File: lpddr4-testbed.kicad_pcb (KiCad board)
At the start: 6 copper layers, 69.6 x 30 mm, 2 parts, among them J1 ddr4-sodimm-edge-connector, U1 MT53E256M16D1

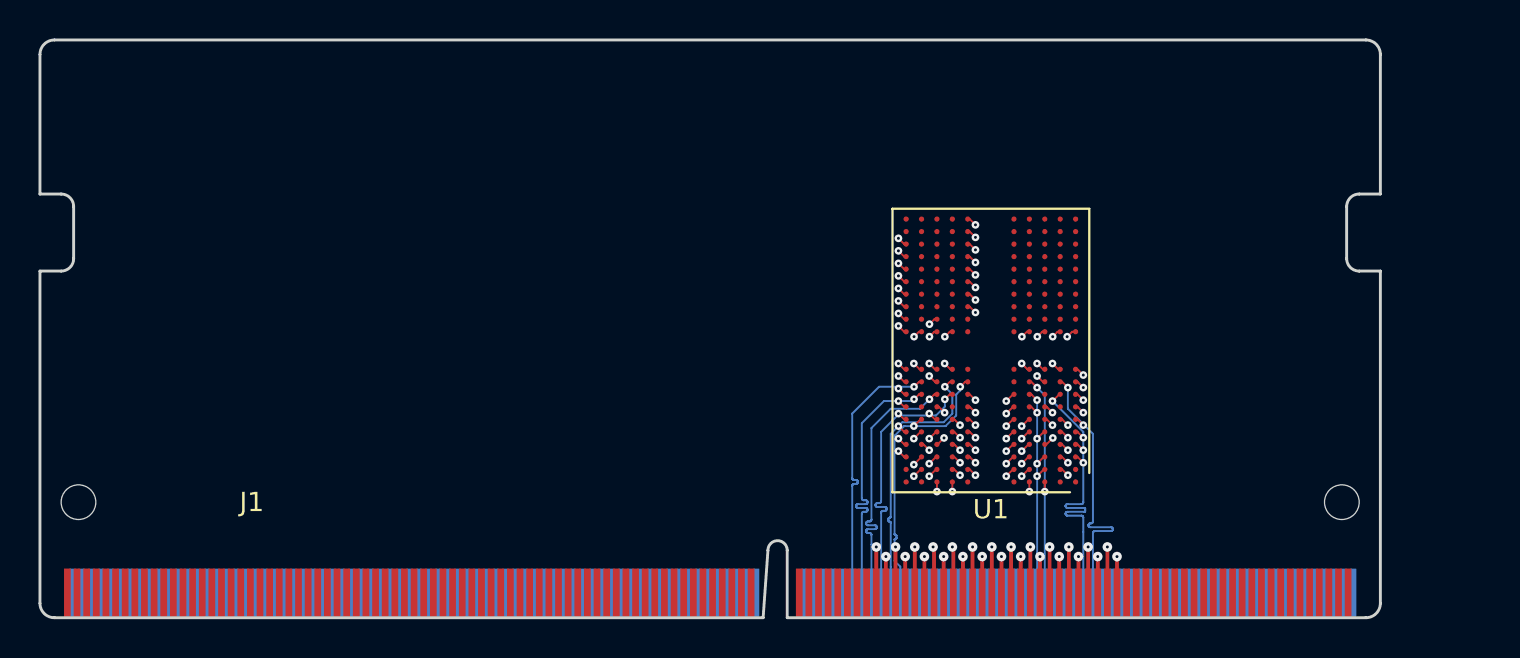
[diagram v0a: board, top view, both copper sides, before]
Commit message: Add vias for power distribution
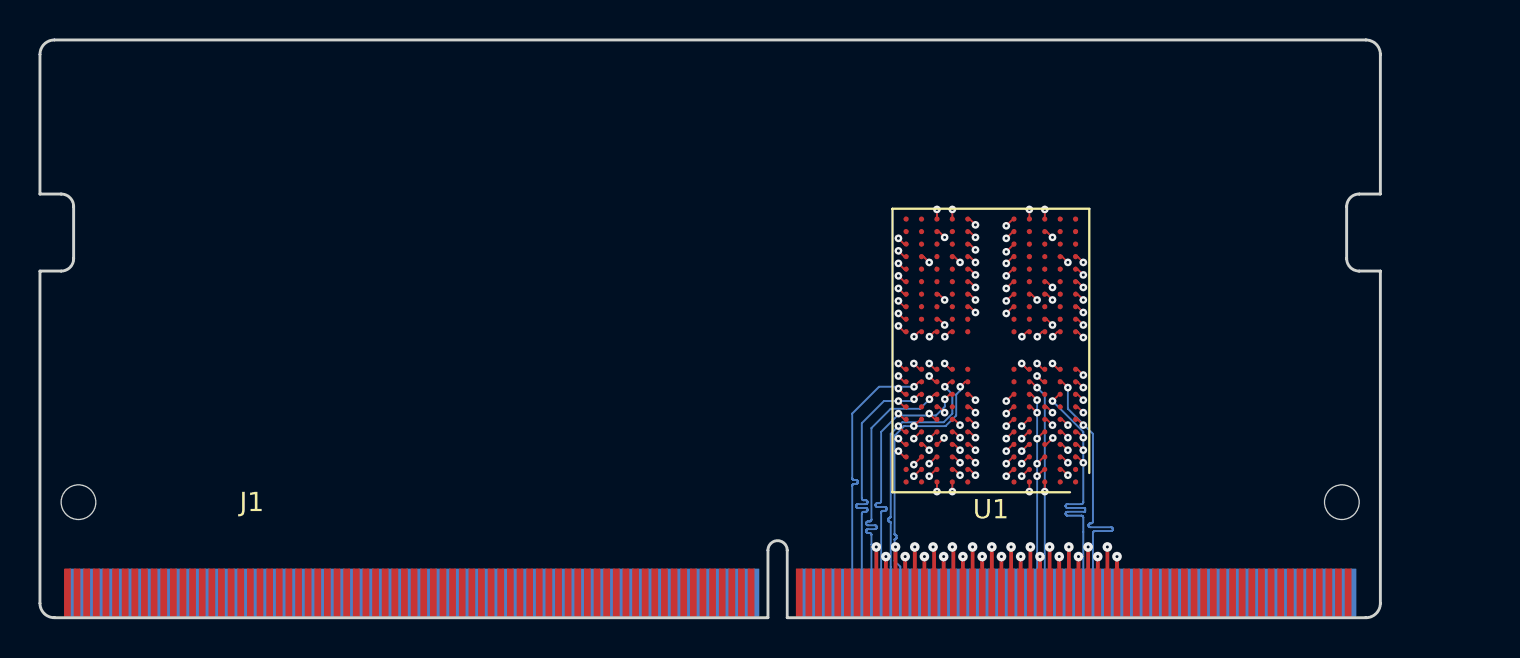
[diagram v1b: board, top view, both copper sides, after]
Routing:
- net GND: track 30.2 -> 38.1 mm, vias 45 -> 60
- net VDDQ: track 6.35 -> 9.54 mm, vias 12 -> 18
- net VDD2: track 9.92 -> 12.6 mm, vias 19 -> 24
- net VDD1: track 2.10 -> 3.15 mm, vias 4 -> 6
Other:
- outline, holes or cut-outs redrawn

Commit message: Add filtering caps to VDDQ
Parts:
- added C1: C_100n_0201, antmicro-footprints:0201-res, B.Cu at (149.8, 93.6)
- added C10: C_100n_0201, antmicro-footprints:0201-res, F.Cu at (142.2, 81.2)
- added C11: C_100n_0201, antmicro-footprints:0201-res, F.Cu at (156.6, 81.9)
- added C12: C_100n_0201, antmicro-footprints:0201-res, F.Cu at (142.3, 91.0)
- added C13: C_100n_0201, antmicro-footprints:0201-res, B.Cu at (152.6, 81.4)
- added C14: C_100n_0201, antmicro-footprints:0201-res, F.Cu at (165.2, 86.9)
- added C15: C_100n_0201, antmicro-footprints:0201-res, B.Cu at (149.4, 81.9)
- added C16: C_100n_0201, antmicro-footprints:0201-res, F.Cu at (162.8, 90.4)
- added C2: C_100n_0201, antmicro-footprints:0201-res, B.Cu at (149.4, 80.0)
- added C3: C_100n_0201, antmicro-footprints:0201-res, B.Cu at (148.9, 93.6)
- added C4: C_100n_0201, antmicro-footprints:0201-res, B.Cu at (147.0, 81.3)
- added C5: C_100n_0201, antmicro-footprints:0201-res, B.Cu at (149.4, 91.0)
- added C6: C_100n_0201, antmicro-footprints:0201-res, B.Cu at (146.3, 83.1)
- added C7: C_100n_0201, antmicro-footprints:0201-res, B.Cu at (145.6, 92.0)
- added C8: C_100n_0201, antmicro-footprints:0201-res, B.Cu at (153.3, 83.2)
- added C9: C_100n_0201, antmicro-footprints:0201-res, F.Cu at (156.4, 91.7)
- added R1: R_10k_0402, antmicro-footprints:0402-res, F.Cu at (126.5, 87.4)
- added R2: R_0R_0402, antmicro-footprints:0402-res, F.Cu at (126.5, 89.4)
- added R3: R_10k_0402, antmicro-footprints:0402-res, F.Cu at (129.4, 87.4)
- added R4: R_10k_0402, antmicro-footprints:0402-res, F.Cu at (129.4, 89.4)
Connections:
- U1 pad G2: /LPDDR4/ODT0_A -> Net-(R1-Pad2)
- U1 pad R4: Net-(U1-PadR4) -> CS0_B
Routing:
- net VDDQ: track 9.54 -> 30.7 mm, vias 18 -> 19
- net GND: track 38.1 -> 56.8 mm, vias 60 -> 62
- net CKE0_A: track 11.3 -> 12.5 mm
- net CS0_A: track 10.6 -> 11.4 mm

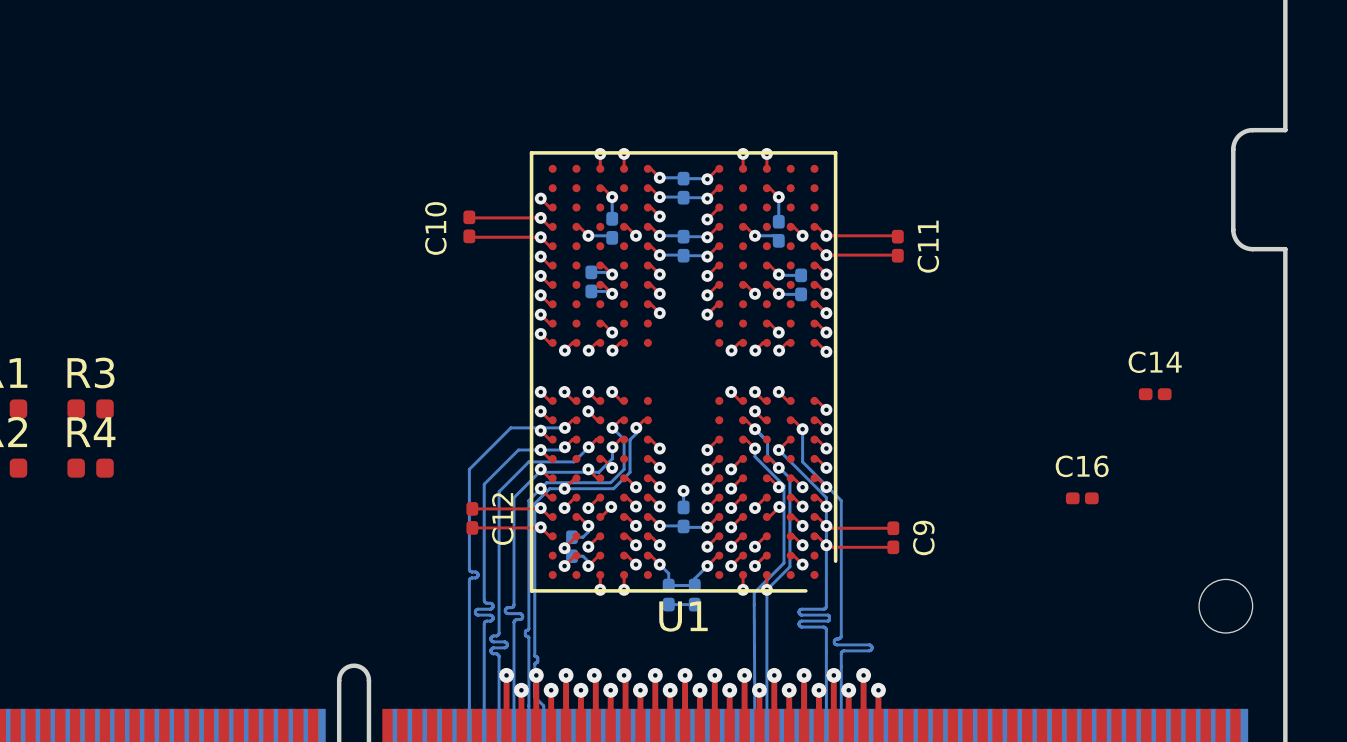
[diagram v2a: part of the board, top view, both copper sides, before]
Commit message: Add Filtering to VCC1
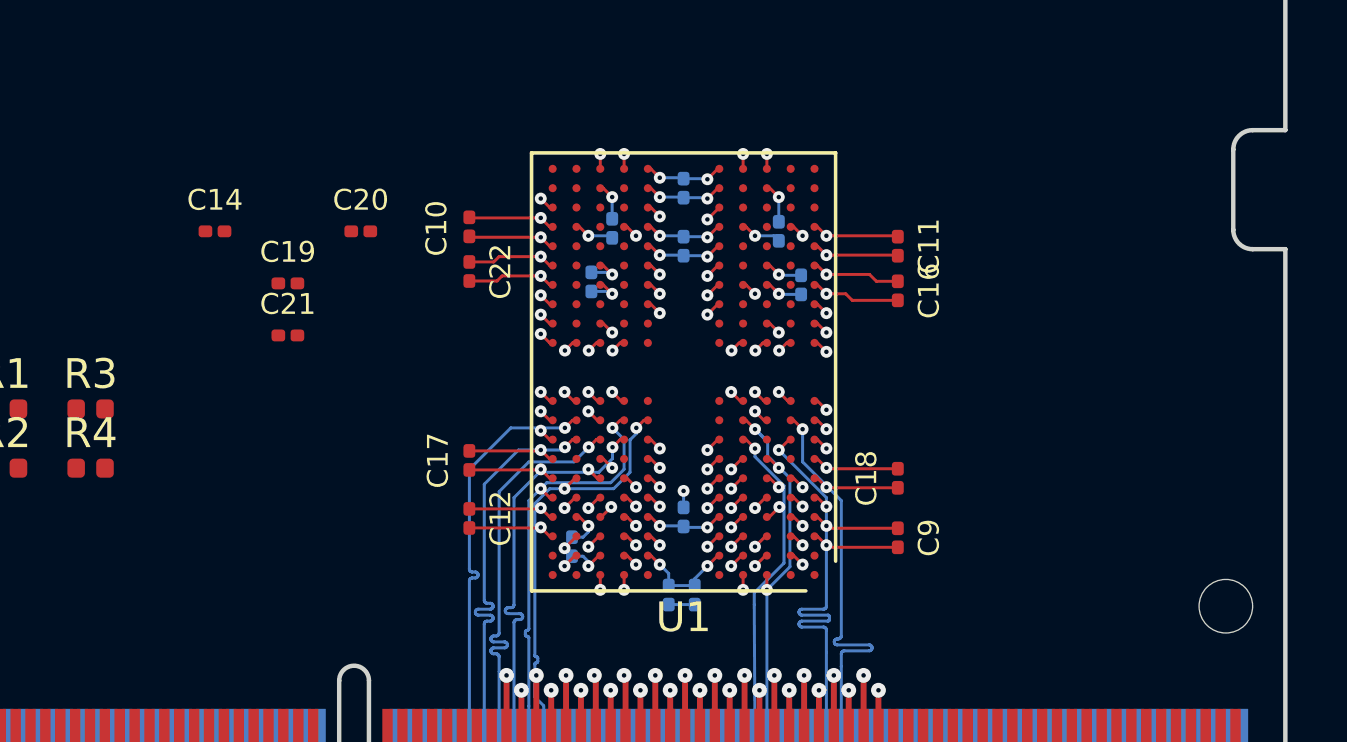
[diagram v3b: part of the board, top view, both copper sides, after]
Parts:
- added C17: C_100n_0201, antmicro-footprints:0201-res, F.Cu at (142.2, 89.1)
- added C18: C_100n_0201, antmicro-footprints:0201-res, F.Cu at (156.6, 89.7)
- added C19: C_100n_0201, antmicro-footprints:0201-res, F.Cu at (136.1, 83.2)
- added C20: C_100n_0201, antmicro-footprints:0201-res, F.Cu at (138.5, 81.4)
- added C21: C_100n_0201, antmicro-footprints:0201-res, F.Cu at (136.1, 84.9)
- added C22: C_100n_0201, antmicro-footprints:0201-res, F.Cu at (142.2, 82.8)
- moved C14 32.1 mm to (133.6, 81.4)
- moved C16 9.33 mm to (156.6, 83.4), turned to 270 degrees
- moved C9 0.15 mm to (156.6, 91.7)
- moved C12 0.10 mm to (142.2, 91.0)
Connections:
- C14 pad 1: VDDQ -> VDD1
- C16 pad 1: VDDQ -> VDD1
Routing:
- net VDD1: track 3.17 -> 13.0 mm
- net GND: track 56.8 -> 66.6 mm

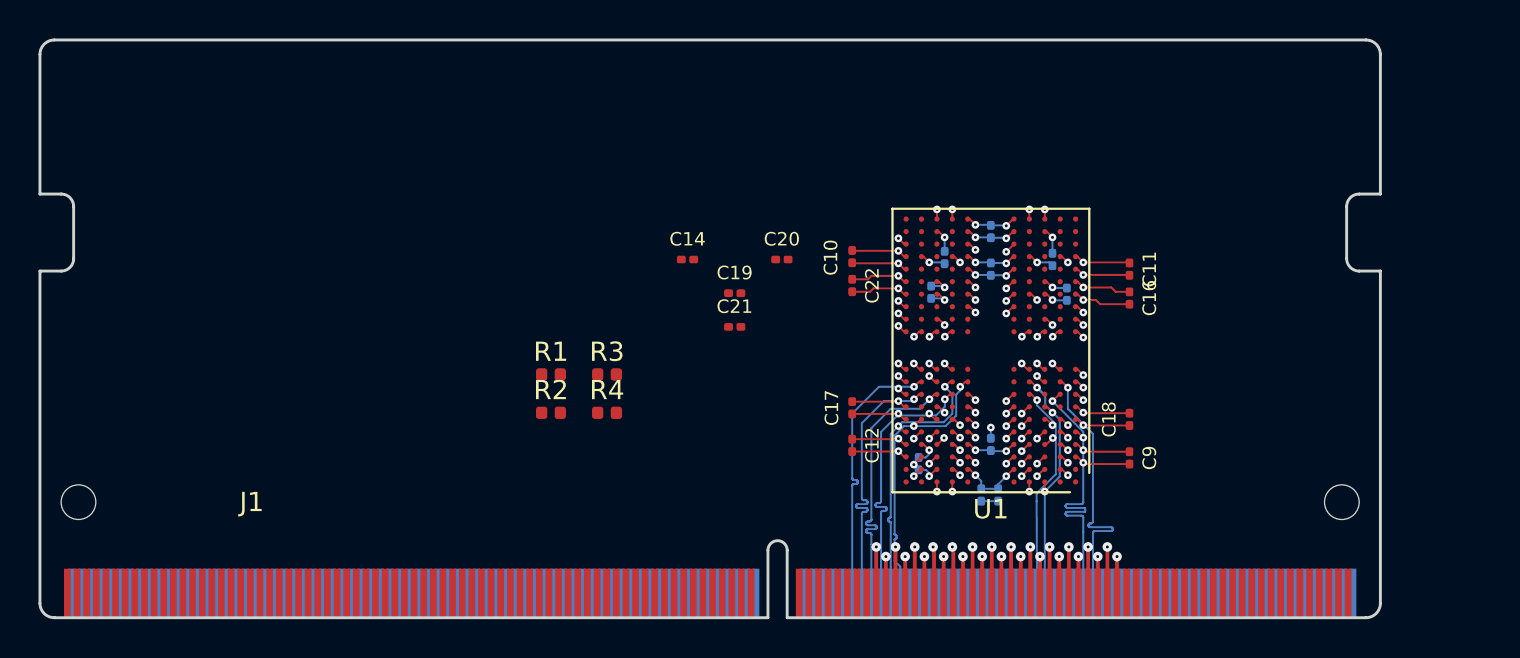
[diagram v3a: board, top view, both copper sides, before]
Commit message: Add filtering to VDD1
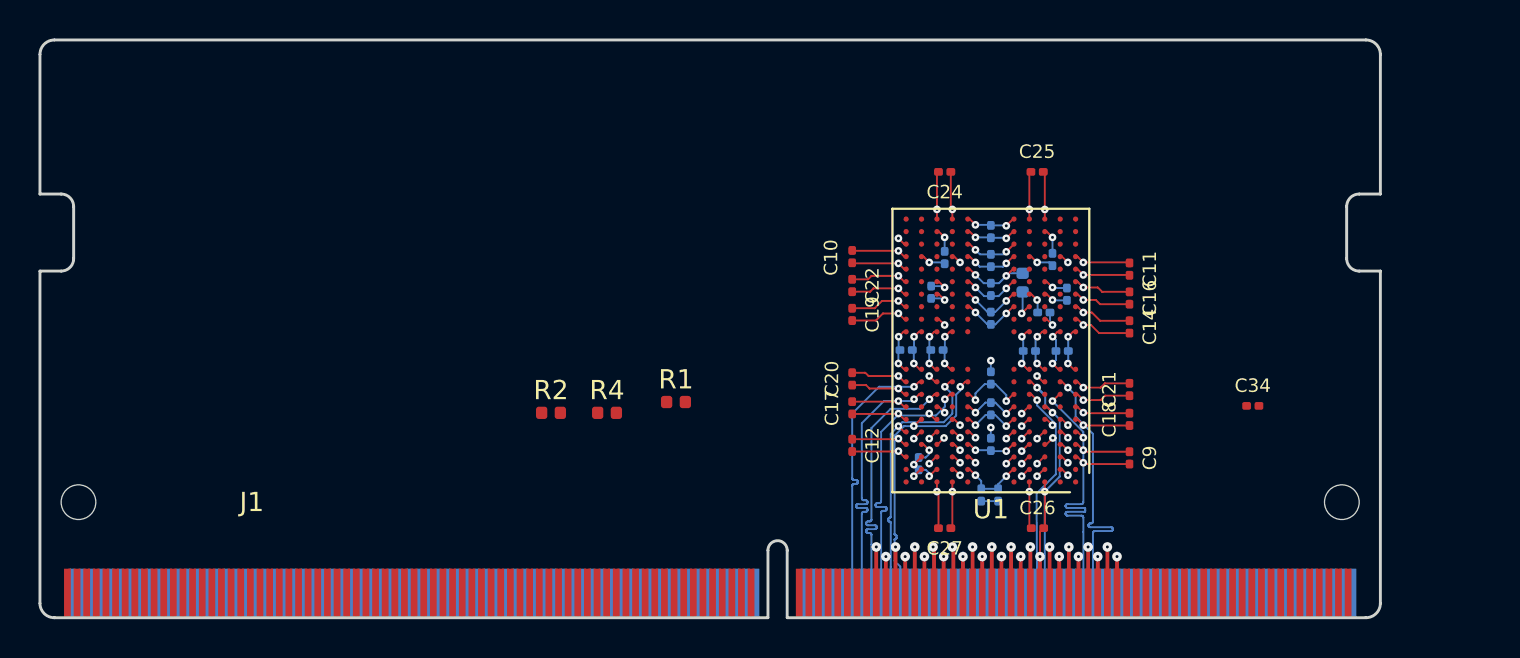
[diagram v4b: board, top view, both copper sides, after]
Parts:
- added C23: C_100n_0201, antmicro-footprints:0201-res, B.Cu at (152.1, 84.2)
- added C24: C_100n_0201, antmicro-footprints:0201-res, F.Cu at (147.0, 76.8)
- added C25: C_100n_0201, antmicro-footprints:0201-res, F.Cu at (151.8, 76.8)
- added C26: C_100n_0201, antmicro-footprints:0201-res, F.Cu at (151.8, 95.3)
- added C27: C_100n_0201, antmicro-footprints:0201-res, F.Cu at (147.0, 95.3)
- added C28: C_100n_0201, antmicro-footprints:0201-res, B.Cu at (149.4, 89.2)
- added C29: C_100n_0201, antmicro-footprints:0201-res, B.Cu at (149.4, 87.5)
- added C30: C_100n_0201, antmicro-footprints:0201-res, B.Cu at (153.1, 86.2)
- added C31: C_100n_0201, antmicro-footprints:0201-res, B.Cu at (151.4, 86.2)
- added C32: C_100n_0201, antmicro-footprints:0201-res, B.Cu at (149.4, 83.0)
- added C33: C_100n_0201, antmicro-footprints:0201-res, B.Cu at (149.4, 84.5)
- added C34: C_100n_0201, antmicro-footprints:0201-res, F.Cu at (163.0, 89.0)
- added C35: C_100n_0201, antmicro-footprints:0201-res, B.Cu at (145.0, 86.1)
- added C36: C_100n_0201, antmicro-footprints:0201-res, B.Cu at (146.6, 86.1)
- R3: moved to B.Cu
- moved C14 23.2 mm to (156.6, 84.9), turned to 270 degrees
- moved R3 22.1 mm to (151.0, 82.6), turned to 90 degrees
- moved C21 20.8 mm to (156.6, 88.2), turned to 90 degrees
- moved C20 7.19 mm to (142.2, 87.6), turned to 90 degrees
- moved R1 6.65 mm to (133.0, 88.8)
- moved C19 6.20 mm to (142.2, 84.2), turned to 270 degrees
- moved C15 0.45 mm to (149.4, 81.5), turned to 90 degrees
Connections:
- C14 pad 1: VDD1 -> VDD2
- C19 pad 1: VDD1 -> VDD2
- C20 pad 1: VDD1 -> VDD2
- C21 pad 1: VDD1 -> VDD2
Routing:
- net GND: track 66.6 -> 100.5 mm, vias 62 -> 63
- net VDD2: track 12.6 -> 45.0 mm
- net CS0_B: track 0.00 -> 1.68 mm, vias 0 -> 1
- net VDD1: track 13.0 -> 13.6 mm

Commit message: Route power planes
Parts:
- C1: moved to F.Cu
- moved R2 47.2 mm to (173.6, 86.7), turned to 180 degrees
- moved R1 40.5 mm to (173.5, 87.8)
- moved C34 10.3 mm to (173.3, 89.2)
- moved C1 6.84 mm to (156.6, 93.2), turned to 90 degrees
- moved C23 4.49 mm to (148.1, 86.1)
- moved R4 1.90 mm to (128.7, 91.1)
- moved C3 1.23 mm to (149.4, 92.5), turned to 90 degrees
- moved R3 0.90 mm to (151.8, 83.1)
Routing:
- net VDD1: track 13.6 -> 87.5 mm, vias 6 -> 10
- net VDD2: track 45.0 -> 55.3 mm, vias 24 -> 30
- net GND: track 100.5 -> 108.8 mm, vias 63 -> 65
- net VDDQ: track 30.9 -> 35.9 mm, vias 19 -> 33
- net CA4_A: track 14.0 -> 12.5 mm
- net CA2_A: track 14.0 -> 12.9 mm
- net CA3_A: track 14.0 -> 12.9 mm
- net (no net): track 0.54 -> 0.00 mm, vias 1 -> 0
- net CS0_B: track 1.68 -> 1.14 mm
- added copper zone on F.Cu, net VDD2
- added copper zone on In3.Cu, net VDD2
- added copper zone on B.Cu, net VDDQ
- added copper zone on In3.Cu, net VDDQ
